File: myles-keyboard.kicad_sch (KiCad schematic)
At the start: 50 parts, among them J1 TRRS, J2 OLED, SW01 Key, SW02 Key, SW03 Key, SW04 Key, SW11 Key, SW12 Key, SW13 Key, SW14 Key, SW15 Key, SW16 Key, SW17 Key, SW18 Key, SW19 Key, SW21 Key, SW22 Key, SW23 Key, SW24 Key, SW25 Key, SW26 Key, SW27 Key, SW28 Key, SW29 Key, SW30 Key, SW31 Key, SW32 Key, SW33 Key, SW34 Key, SW35 Key, SW36 Key, SW37 Key, SW38 Key, SW39 Key, SW40 Key, SW41 Key, SW42 Key, SW43 Key, SW44 Key, SW45 Key, SW46 Key, SW47 Key, SW48 Key, SW49 Key, U1 ProMicro

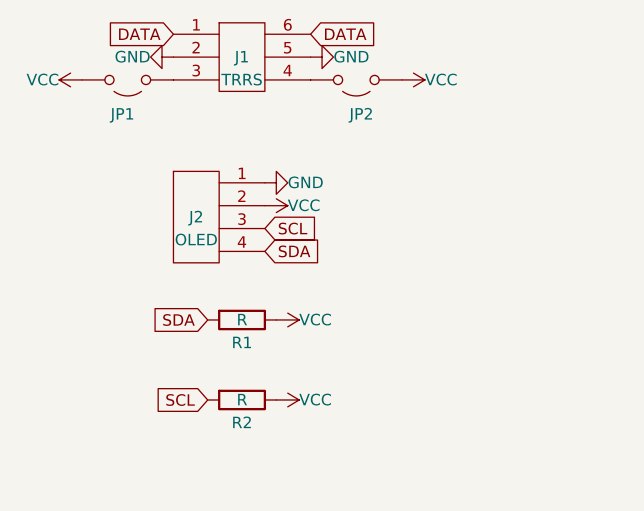
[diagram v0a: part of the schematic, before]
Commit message: added new jumpers
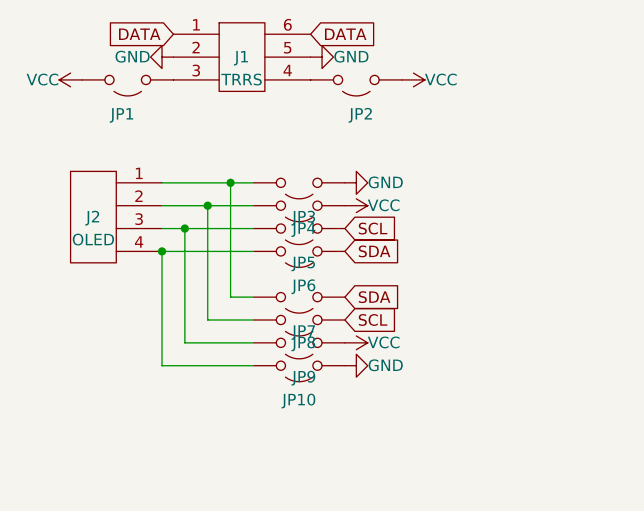
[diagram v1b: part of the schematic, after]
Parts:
- removed R1, R2: R, myles-keyboard:R, symbol Device:R
- added JP10, JP3, JP4, JP5, JP6, JP7, JP8, JP9: Jumper_2_Open, myles-keyboard:Jumper, symbol Jumper:Jumper_2_Open
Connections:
- net GND: now also JP10.1 (A), JP3.1 (A); no longer J2.1
- net SCL: now also JP5.1 (A), JP8.1 (A); no longer J2.3
- net SDA: now also JP6.1 (A), JP7.1 (A); no longer J2.4
- net VCC: now also JP4.1 (A), JP9.1 (A); no longer J2.2
- new net: J2.1, JP3.2 (B), JP7.2 (B)
- new net: J2.3, JP5.2 (B), JP9.2 (B)
- new net: J2.4, JP10.2 (B), JP6.2 (B)
- new net: J2.2, JP4.2 (B), JP8.2 (B)
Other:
- moved on the sheet: J2

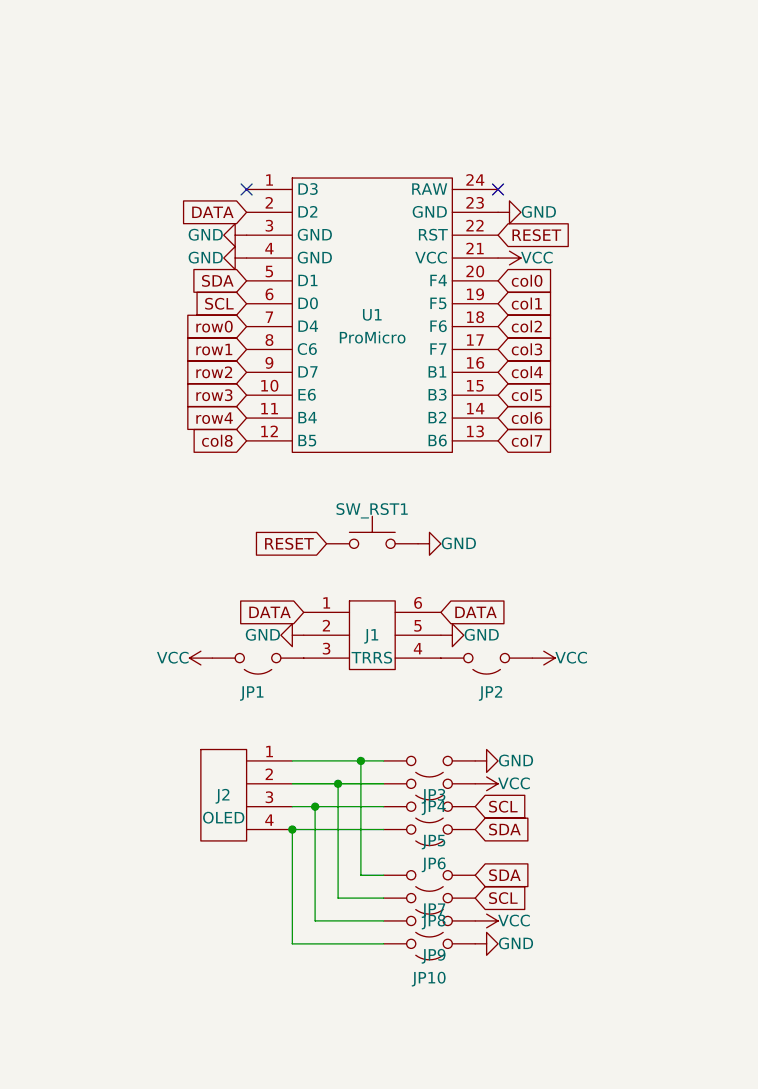
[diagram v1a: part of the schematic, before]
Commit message: rearrange TRRS jack
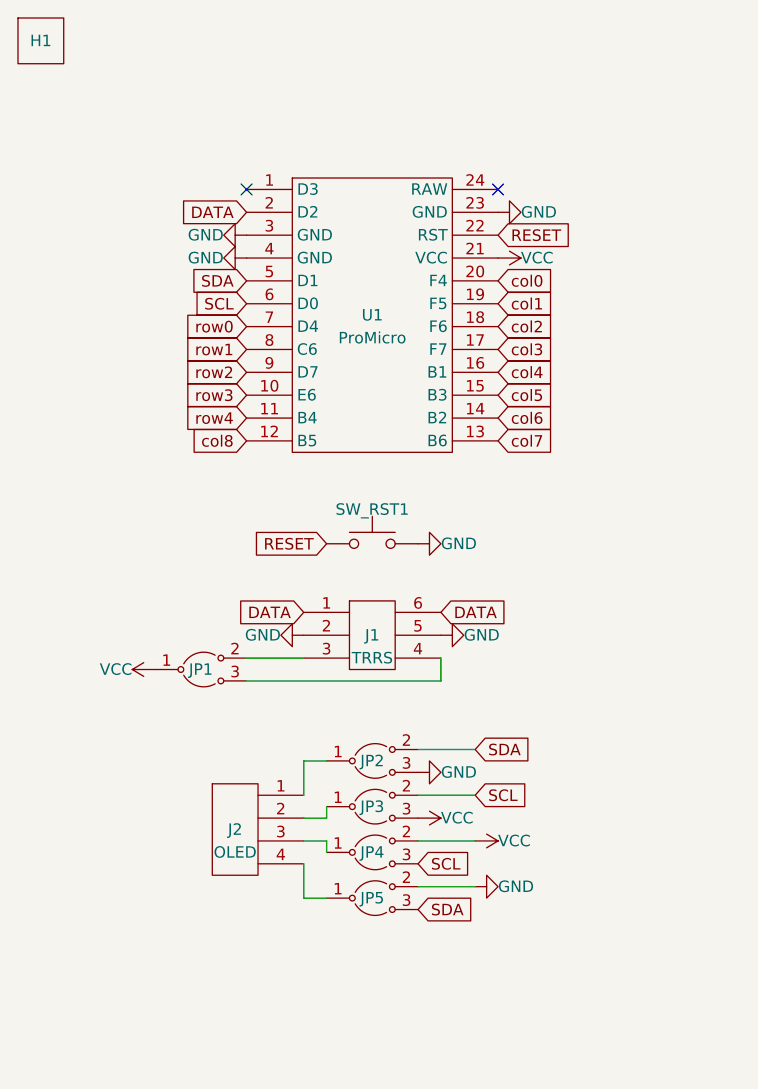
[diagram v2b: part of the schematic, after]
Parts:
- removed JP1, JP10, JP2, JP3, JP4, JP5, JP6, JP7, JP8, JP9: Jumper_2_Open, myles-keyboard:Jumper, symbol Jumper:Jumper_2_Open
- added H1: ~, myles-keyboard:RightPlate, symbol myles-keyboard:RightPate
- added JP1, JP2, JP3, JP4, JP5: ~, myles-keyboard:Jumper, symbol myles-keyboard:Jumper
- SW_RST1: footprint myles-keyboard:MJTP1117 -> myles-keyboard:PTS636
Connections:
- net GND: now also JP2.3, JP5.2
- net SCL: now also JP3.2, JP4.3
- net SDA: now also JP2.2, JP5.3
- net VCC: now also JP1.1, JP3.3, JP4.2
- net at J2.1: now also JP2.1
- net at J2.3: now also JP4.1
- net at J2.4: now also JP5.1
- net at J1.3: now also JP1.2
- net at J1.4: now also JP1.3
- net at J2.2: now also JP3.1
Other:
- moved on the sheet: J2

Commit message: reorder jumpers
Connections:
- net GND: now also JP2.1; no longer JP2.3, JP5.2
- net SCL: now also JP4.1; no longer JP3.2, JP4.3
- net SDA: now also JP5.1; no longer JP2.2, JP5.3
- net VCC: now also JP3.1; no longer JP3.3, JP4.2
- net at J2.1: now also JP2.3, JP5.2; no longer JP2.1
- net at J2.2: now also JP3.3, JP4.2; no longer JP3.1
- net at J2.3: now also JP3.2, JP4.3; no longer JP4.1
- net at J2.4: now also JP2.2, JP5.3; no longer JP5.1
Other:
- moved on the sheet: J2, JP2, JP3, JP4, JP5

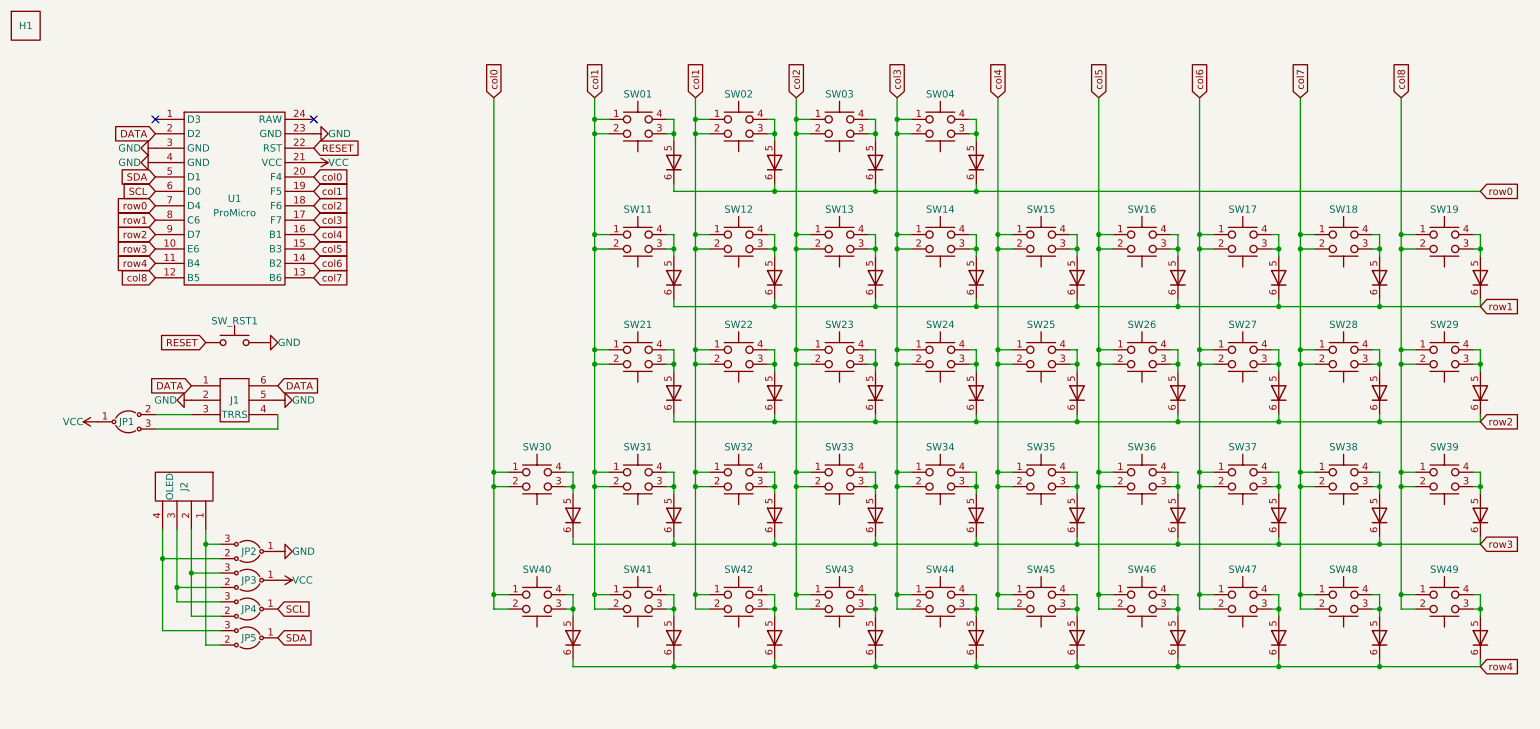
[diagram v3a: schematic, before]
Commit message: add lots of traces
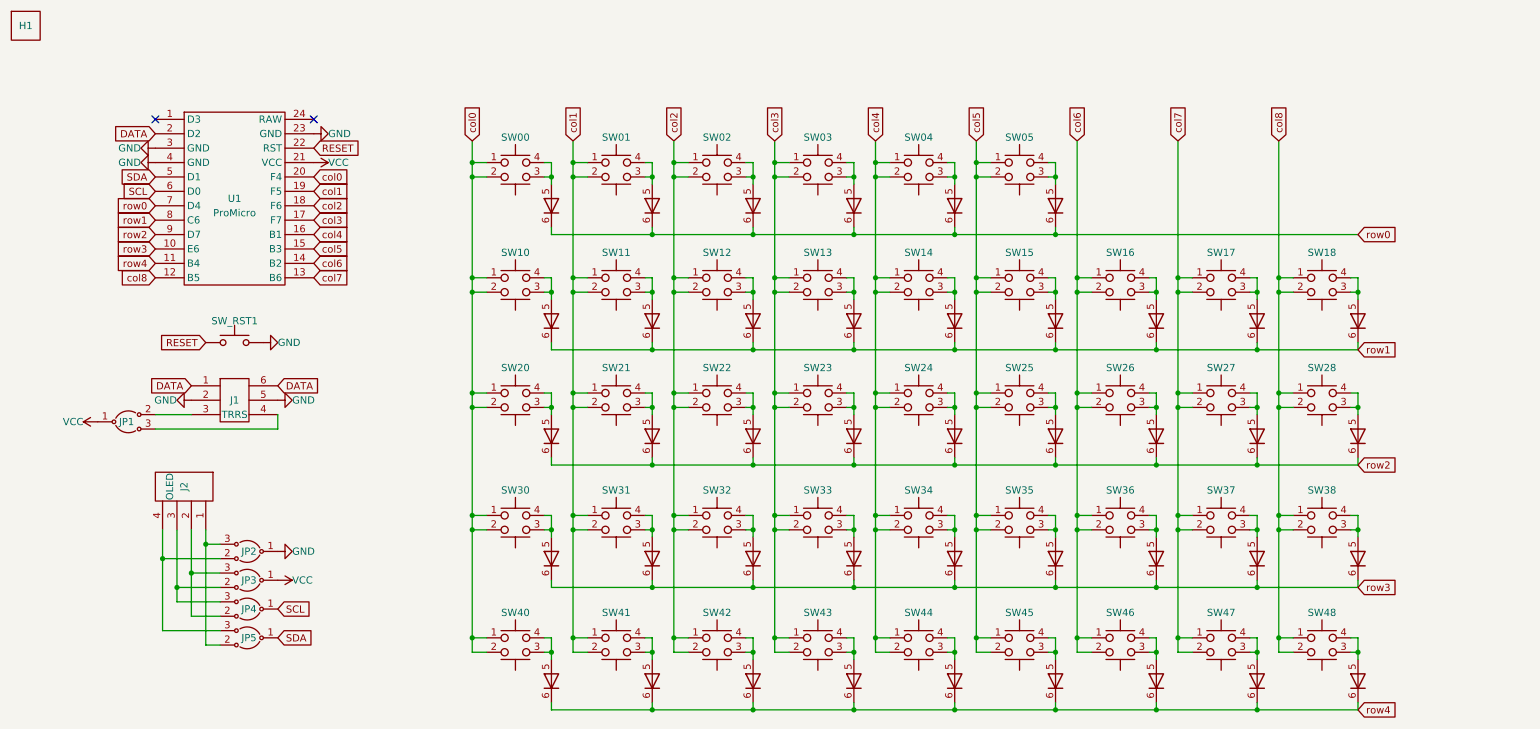
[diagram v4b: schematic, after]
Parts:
- removed SW30, SW40: Key, myles-keyboard:Key, symbol myles-keyboard:Key
- added SW04, SW05: Key, myles-keyboard:KeyLeft, symbol myles-keyboard:Key
- SW00: renamed from SW01; footprint myles-keyboard:Key -> myles-keyboard:KeyLeft
- SW03: renamed from SW04; footprint myles-keyboard:Key -> myles-keyboard:KeyRight
- SW14: renamed from SW15; footprint myles-keyboard:Key -> myles-keyboard:KeyLeft
- SW18: renamed from SW19; footprint myles-keyboard:Key -> myles-keyboard:KeyRight
- SW28: renamed from SW29; footprint myles-keyboard:Key -> myles-keyboard:KeyRight
- SW38: renamed from SW39; footprint myles-keyboard:Key -> myles-keyboard:KeyRight
- SW45: renamed from SW46; footprint myles-keyboard:Key -> myles-keyboard:KeyRight
- SW48: renamed from SW49; footprint myles-keyboard:Key -> myles-keyboard:KeyRight
- renumbered SW02 to SW01, SW03 to SW02, SW11 to SW10, SW12 to SW11, SW13 to SW12, SW14 to SW13, SW16 to SW15, SW17 to SW16, SW18 to SW17, SW21 to SW20, SW22 to SW21, SW23 to SW22, SW24 to SW23, SW25 to SW24, SW26 to SW25, SW27 to SW26, SW28 to SW27, SW31 to SW30, SW32 to SW31, SW33 to SW32, SW34 to SW33, SW35 to SW34, SW36 to SW35, SW37 to SW36, SW38 to SW37, SW41 to SW40, SW42 to SW41, SW43 to SW42, SW44 to SW43, SW45 to SW44, SW47 to SW46, SW48 to SW47
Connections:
- net col0: now also SW00.1, SW00.2, SW10.1, SW10.2, SW20.1, SW20.2, SW30.1, SW30.2, SW40.1, SW40.2
- net col1: no longer SW00.1, SW00.2, SW10.1, SW10.2, SW20.1, SW20.2, SW30.1, SW30.2, SW40.1, SW40.2
- net col4: now also SW04.1, SW04.2
- net col5: now also SW05.1, SW05.2
- net row0: now also SW04.6, SW05.6
- new net: SW04.3, SW04.4, SW04.5
- new net: SW05.3, SW05.4, SW05.5
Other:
- moved on the sheet: SW00, SW01, SW02, SW03, SW10, SW11, SW12, SW13, SW14, SW15, SW16, SW17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

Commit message: draft wiring
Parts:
- SW10, SW20: footprint myles-keyboard:Key -> myles-keyboard:KeyLeft
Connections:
- net col0: now also U1.19 (F5); no longer U1.20 (F4)
- net col1: now also U1.8 (C6); no longer U1.19 (F5)
- net col2: now also U1.9 (D7); no longer U1.18 (F6)
- net col3: now also U1.10 (E6); no longer U1.17 (F7)
- net col4: now also U1.11 (B4); no longer U1.16 (B1)
- net col5: now also U1.12 (B5); no longer U1.15 (B3)
- net col6: now also U1.17 (F7); no longer U1.14 (B2)
- net col7: now also U1.16 (B1); no longer U1.13 (B6)
- net col8: now also U1.15 (B3); no longer U1.12 (B5)
- net row0: now also U1.20 (F4); no longer U1.7 (D4)
- net row1: now also U1.7 (D4); no longer U1.8 (C6)
- net row2: now also U1.18 (F6); no longer U1.9 (D7)
- net row3: now also U1.14 (B2); no longer U1.10 (E6)
- net row4: now also U1.13 (B6); no longer U1.11 (B4)

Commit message: tidy wiring
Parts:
- SW30: footprint myles-keyboard:Key -> myles-keyboard:KeyLeft
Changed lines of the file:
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@@
       (effects (font (size 1.27 1.27)) hide)
     )
-    (property "Footprint" "myles-keyboard:Key" (at 102.87 104.14 0)
+    (property "Footprint" "myles-keyboard:KeyLeft" (at 102.87 104.14 0)
       (effects (font (size 1.27 1.27)) hide)
     )

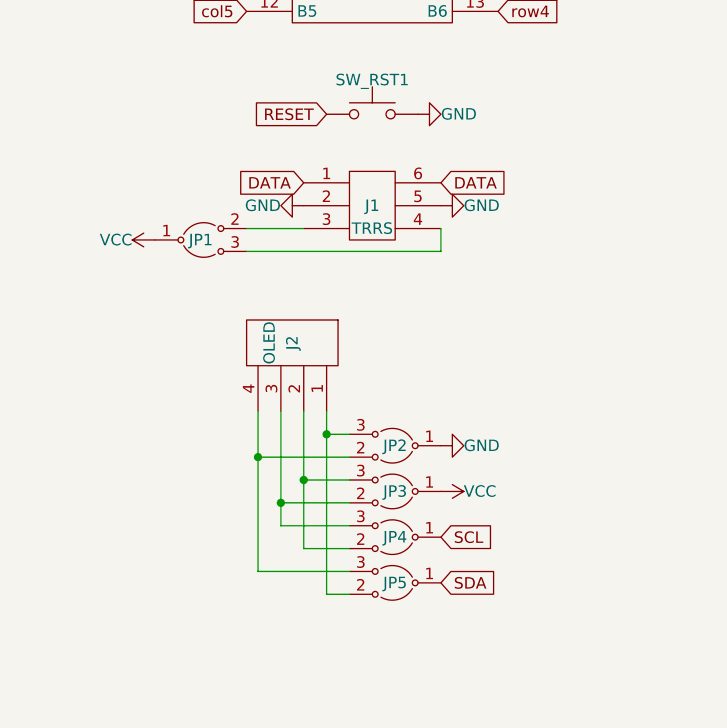
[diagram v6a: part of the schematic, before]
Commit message: remove OLED
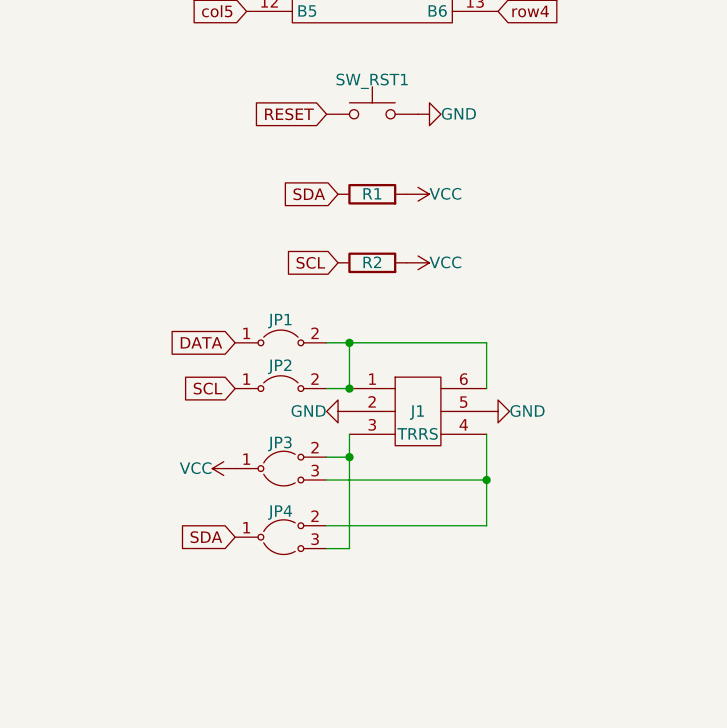
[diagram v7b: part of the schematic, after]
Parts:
- removed J2: OLED, myles-keyboard:OLED, symbol myles-keyboard:OLED
- removed JP3, JP4, JP5: ~, myles-keyboard:Jumper, symbol myles-keyboard:Jumper
- added JP3, JP4: JumperSplit, myles-keyboard:JumperSplit, symbol myles-keyboard:JumperSplit
- added R1, R2: R, myles-keyboard:SDR18, symbol Device:R
- JP1, JP2: value ~ -> Jumper
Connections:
- net DATA: now also JP1.1; no longer J1.1, J1.6
- net GND: no longer JP2.1
- net SCL: now also JP2.1, R2.1
- net SDA: now also JP4.1, R1.1
- net VCC: now also JP3.1, R1.2, R2.2; no longer JP1.1
- net at JP1.2: now also J1.1, J1.6, JP2.2; no longer J1.3
- net at J1.4: now also JP3.3, JP4.2; no longer JP1.3
- new net: J1.3, JP3.2, JP4.3

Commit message: add reset button 3d model and trim 1m off TRRS jack front
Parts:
- removed SW_RST1: SW_Push, myles-keyboard:PTS636, symbol Switch:SW_Push
- added SW_RST1: SW_Push, myles-keyboard:PTS636, symbol myles-keyboard:SW_Push
- H1: value ~ -> RightPlate
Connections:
- net GND: now also SW_RST1.2
- net RESET: now also SW_RST1.1
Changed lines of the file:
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@@
       (effects (font (size 1.27 1.27)))
     )
-    (property "Value" "~" (at 16.51 16.51 0)
-      (effects (font (size 1.27 1.27)))
+    (property "Value" "RightPlate" (at 16.51 16.51 0)
+      (effects (font (size 1.27 1.27)) hide)
     )
     (property "Footprint" "myles-keyboard:RightPlate" (at 16.51 16.51 0)
@@
     )
   )
-  (symbol (lib_id "Switch:SW_Push") (at 53.34 72.39 0) (unit 1)
-    (in_bom yes) (on_board yes) (dnp no) (fields_autoplaced)
-    (property "Reference" "SW_RST1" (at 53.34 68.58 0)
-      (effects (font (size 1.27 1.27)))
-    )
-    (property "Value" "SW_Push" (at 53.34 68.58 0)
-      (effects (font (size 1.27 1.27)) hide)
-    )
-    (property "Footprint" "myles-keyboard:PTS636" (at 53.34 67.31 0)
-      (effects (font (size 1.27 1.27)) hide)
-    )
-    (property "Datasheet" "~" (at 53.34 67.31 0)
-      (effects (font (size 1.27 1.27)) hide)
-    )
-    (pin "1")
-    (pin "2")
-    (instances
-      (project "myles-keyboard"
-        (path "/55a8c568-8b67-4781-bca4-b9ba3160a3cd"
-          (reference "SW_RST1") (unit 1)
-        )
-      )
-    )
-  )
   (symbol (lib_id "power:VCC") (at 38.1 111.76 90) (unit 1)
     (in_bom yes) (on_board yes) (dnp no)
@@
         )
       )
+    )
+  )
+  (symbol (lib_id "myles-keyboard:SW_Push") (at 53.34 72.39 0) (unit 1)
+    (in_bom yes) (on_board yes) (dnp no) (fields_autoplaced)
+    (property "Reference" "SW_RST1" (at 53.34 68.58 0)
+      (effects (font (size 1.27 1.27)))
+    )
+    (property "Value" "SW_Push" (at 53.34 68.58 0)
+      (effects (font (size 1.27 1.27)) hide)
+    )
+    (property "Footprint" "myles-keyboard:PTS636" (at 53.34 67.31 0)
+      (effects (font (size 1.27 1.27)) hide)
+    )
+    (property "Datasheet" "~" (at 53.34 67.31 0)
+      (effects (font (size 1.27 1.27)) hide)
+    )
+    (pin "1")
+    (pin "2")
+    (instances
+      (project "myles-keyboard"
+        (path "/55a8c568-8b67-4781-bca4-b9ba3160a3cd"
+          (reference "SW_RST1") (unit 1)
+        )
+      )
